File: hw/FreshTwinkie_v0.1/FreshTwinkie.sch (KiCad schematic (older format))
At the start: 54 parts, among them J1 USB_B_Micro, J2 USB_C_Receptacle, P1 USB_C_Plug, Q4 BSD840N, SW1 SW_Push, U1 INA260, U2 INA260, U5 STM32F072CBUx

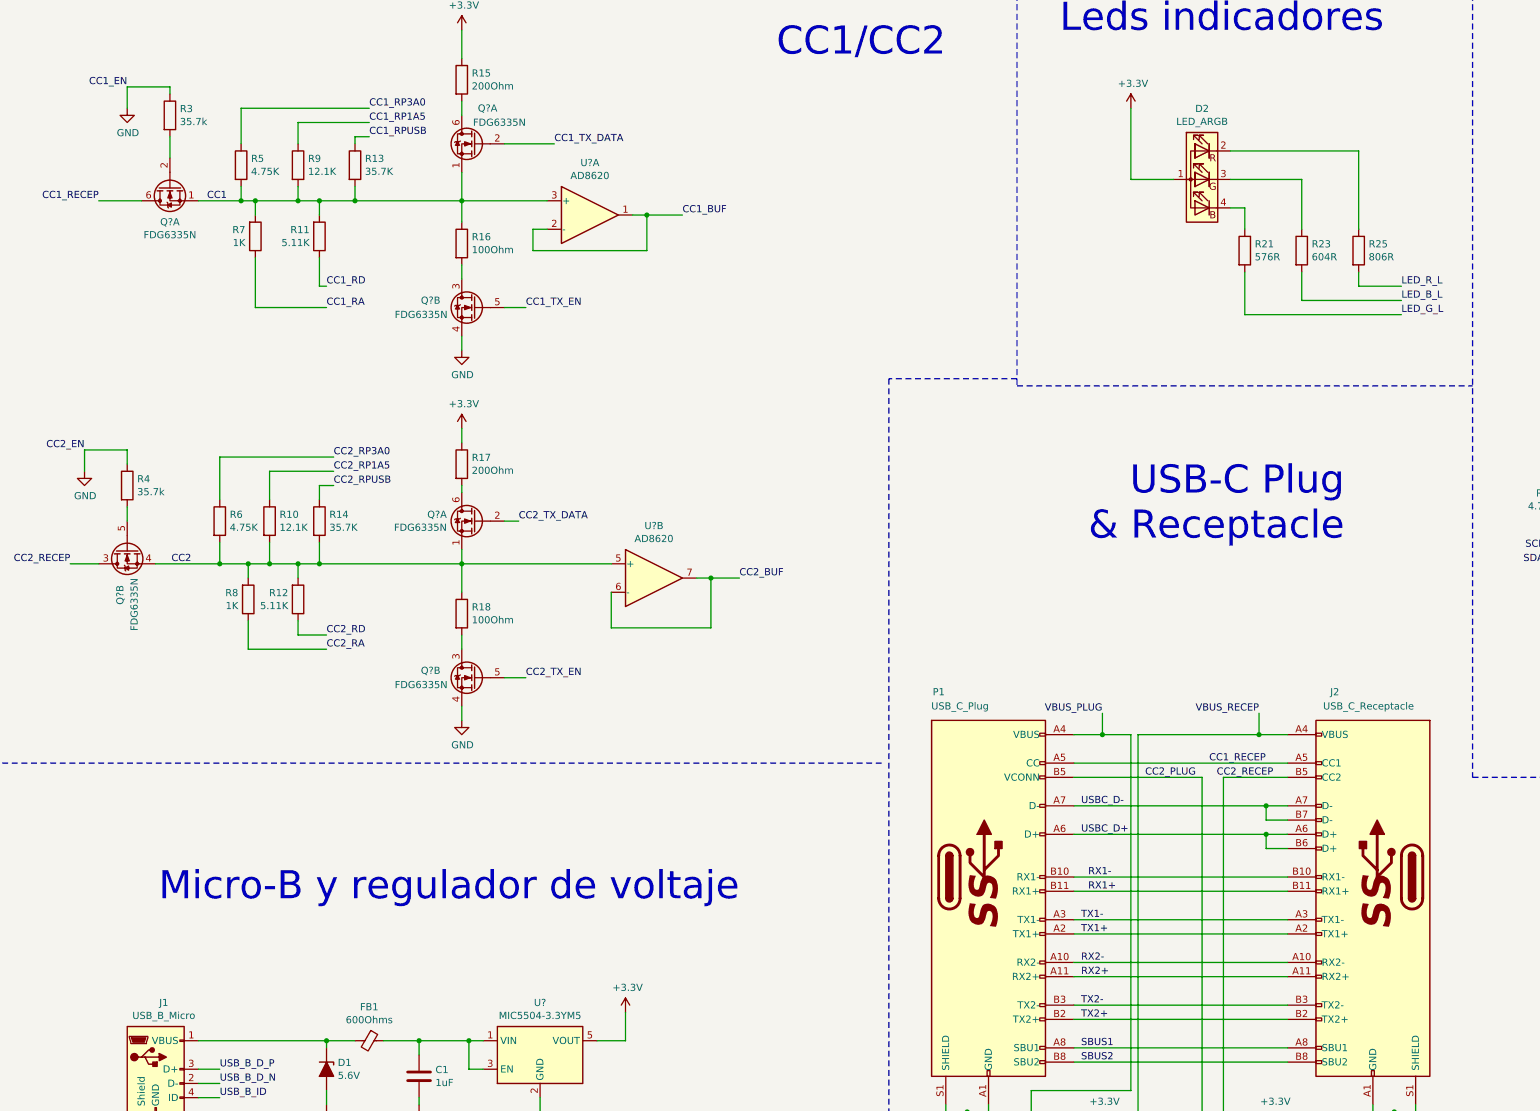
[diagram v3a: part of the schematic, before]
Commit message: changeLEDRvalor
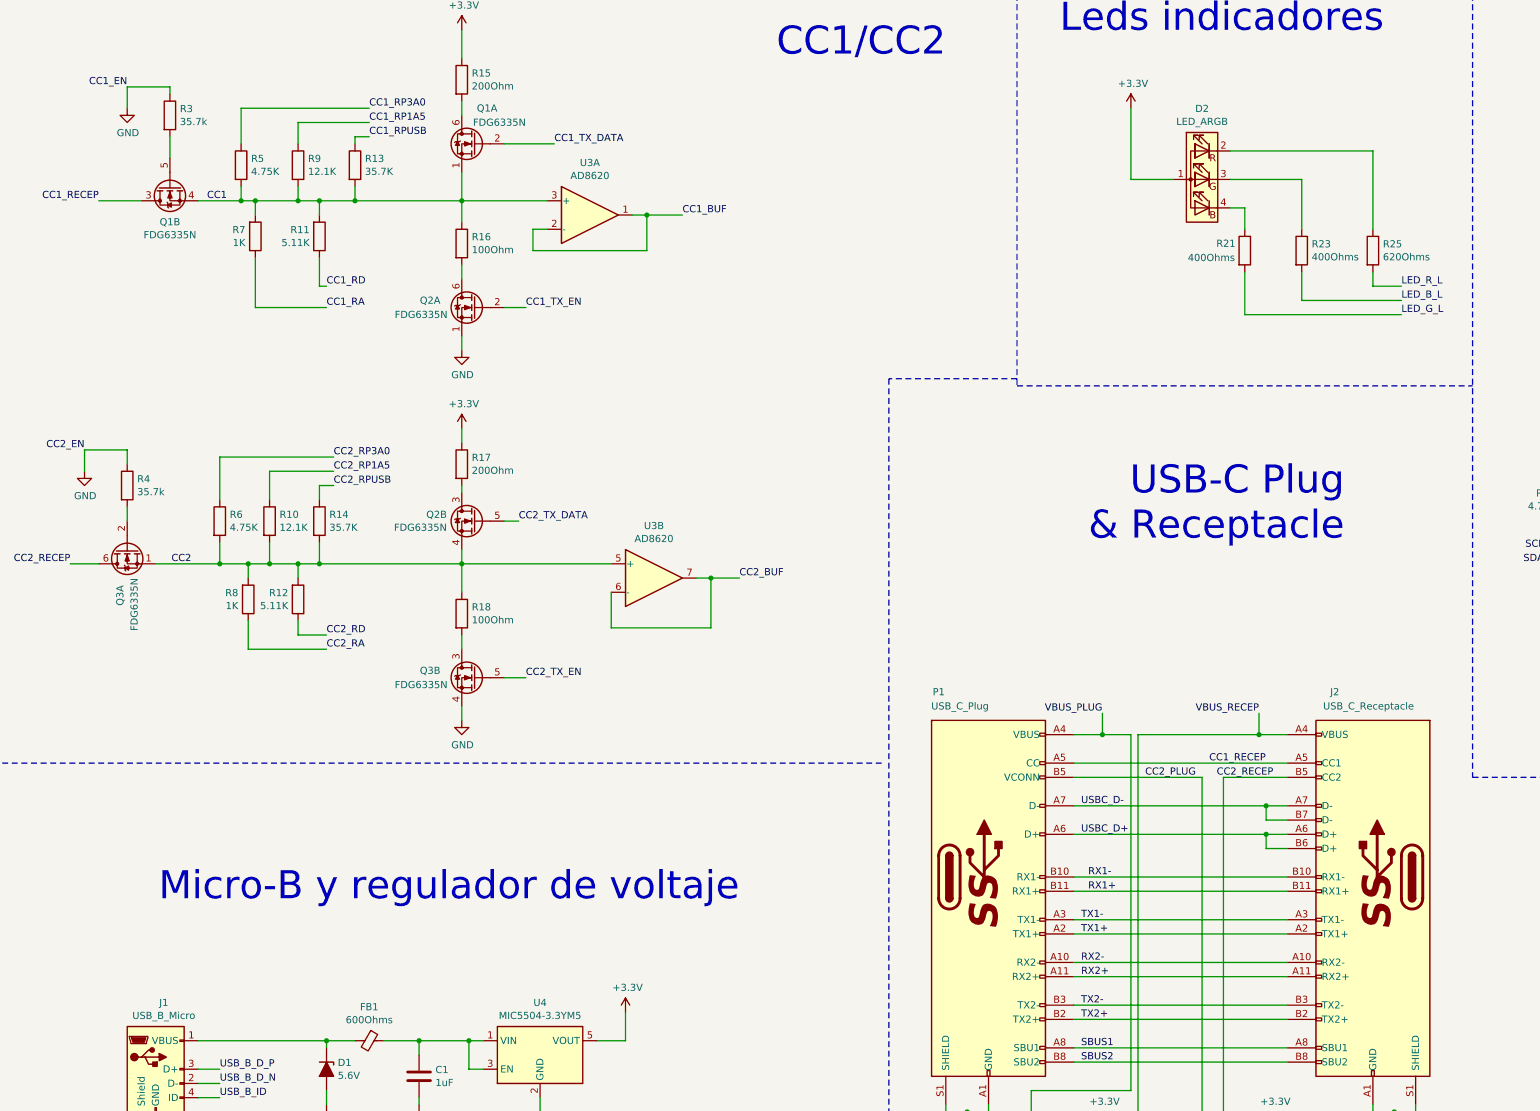
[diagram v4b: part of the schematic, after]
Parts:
- R21: value 576R -> 400Ohms
- R23: value 604R -> 400Ohms
- R25: value 806R -> 620Ohms
- gave numbers to parts that had none: 5
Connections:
- net CC1: now also Q1.4 (S); no longer Q1.1 (S)
- net CC1_RECEP: now also Q1.3 (D); no longer Q1.6 (D)
- net CC1_TX_EN: now also Q2.2 (G); no longer Q2.5 (G)
- net CC2: now also Q2.4 (S), Q3.1 (S); no longer Q2.1 (S), Q3.4 (S)
- net CC2_RECEP: now also Q3.6 (D); no longer Q3.3 (D)
- net CC2_TX_DATA: now also Q2.5 (G); no longer Q2.2 (G)
- net GND: now also Q2.1 (S); no longer Q2.4 (S)
- net at R3.2: now also Q1.5 (G); no longer Q1.2 (G)
- net at R16.2: now also Q2.6 (D); no longer Q2.3 (D)
- net at R4.2: now also Q3.2 (G); no longer Q3.5 (G)
- net at R17.2: now also Q2.3 (D); no longer Q2.6 (D)
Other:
- moved on the sheet: R25
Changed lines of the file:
@@
 U 1 1 5CA5AD96
 P 9600 2500
-F 0 "R21" H 9670 2546 50  0000 L CNN
-F 1 "576R" H 9670 2455 50  0000 L CNN
+F 0 "R21" H 9400 2550 50  0000 L CNN
+F 1 "400Ohms" H 9200 2450 50  0000 L CNN
 F 2 "gkl_dipol:R_0201" V 9530 2500 50  0001 C CNN
 F 3 "~" H 9600 2500 50  0001 C CNN
@@
 P 10000 2500
 F 0 "R23" H 10070 2546 50  0000 L CNN
-F 1 "604R" H 10070 2455 50  0000 L CNN
+F 1 "400Ohms" H 10070 2455 50  0000 L CNN
 F 2 "gkl_dipol:R_0201" V 9930 2500 50  0001 C CNN
 F 3 "~" H 10000 2500 50  0001 C CNN
@@
 L Device:R R25
 U 1 1 5CA5BD82
-P 10400 2500
-F 0 "R25" H 10470 2546 50  0000 L CNN
-F 1 "806R" H 10470 2455 50  0000 L CNN
-F 2 "gkl_dipol:R_0201" V 10330 2500 50  0001 C CNN
-F 3 "~" H 10400 2500 50  0001 C CNN
-F 4 "RC0201FR-07806RL" H 10400 2500 50  0001 C CNN "PN"
-F 5 "Yageo" H 10400 2500 50  0001 C CNN "Mfg"
-	1    10400 2500
+P 10500 2500
+F 0 "R25" H 10570 2546 50  0000 L CNN
+F 1 "620Ohms" H 10570 2455 50  0000 L CNN
+F 2 "gkl_dipol:R_0201" V 10430 2500 50  0001 C CNN
+F 3 "~" H 10500 2500 50  0001 C CNN
+F 4 "RC0201FR-07806RL" H 10500 2500 50  0001 C CNN "PN"
+F 5 "Yageo" H 10500 2500 50  0001 C CNN "Mfg"
+	1    10500 2500
 	1    0    0    -1
 $EndComp
@@
 	10000 2000 10000 2350
 Wire Wire Line
-	9500 1800 10400 1800
-Wire Wire Line
-	10400 1800 10400 2350
-Wire Wire Line
-	10400 2650 10400 2750
-Wire Wire Line
-	10400 2750 10700 2750
+	10500 2750 10700 2750
 Text Label 10700 2750 0    50   ~ 0
 LED_R_L
@@
 SBUS2
 $Comp
-L power:+3.3V #PWR?
+L power:+3.3V #PWR023
 U 1 1 60DEF09B
 P 9800 8650
-F 0 "#PWR?" H 9800 8500 50  0001 C CNN
+F 0 "#PWR023" H 9800 8500 50  0001 C CNN
 F 1 "+3.3V" H 9815 8823 50  0000 C CNN
 F 2 "" H 9800 8650 50  0001 C CNN
@@
 	9800 8650 9800 8700
 $Comp
-L power:GND #PWR?
+L power:GND #PWR027
 U 1 1 60E1F5E6
 P 9800 9550
-F 0 "#PWR?" H 9800 9300 50  0001 C CNN
+F 0 "#PWR027" H 9800 9300 50  0001 C CNN
 F 1 "GND" H 9805 9377 50  0000 C CNN
 F 2 "" H 9800 9550 50  0001 C CNN
@@
 	9800 9550 9800 9500
 $Comp
-L power:+3.3V #PWR?
+L power:+3.3V #PWR022
 U 1 1 60E77EB5
 P 8600 8650
-F 0 "#PWR?" H 8600 8500 50  0001 C CNN
+F 0 "#PWR022" H 8600 8500 50  0001 C CNN
 F 1 "+3.3V" H 8615 8823 50  0000 C CNN
 F 2 "" H 8600 8650 50  0001 C CNN
@@
 $EndComp
 $Comp
-L power:GND #PWR?
+L power:GND #PWR026
 U 1 1 60E78743
 P 8600 9550
-F 0 "#PWR?" H 8600 9300 50  0001 C CNN
+F 0 "#PWR026" H 8600 9300 50  0001 C CNN
 F 1 "GND" H 8605 9377 50  0000 C CNN
 F 2 "" H 8600 9550 50  0001 C CNN
@@
 	9300 9000 9400 9000
 $Comp
-L power:GND #PWR?
+L power:GND #PWR021
 U 1 1 60F8E5E0
 P 10650 8600
-F 0 "#PWR?" H 10650 8350 50  0001 C CNN
+F 0 "#PWR021" H 10650 8350 50  0001 C CNN
 F 1 "GND" H 10655 8427 50  0000 C CNN
 F 2 "" H 10650 8600 50  0001 C CNN
@@
 	10650 8550 10800 8550
 $Comp
-L power:GND #PWR?
+L power:GND #PWR020
 U 1 1 60FBB0CD
 P 7650 8600
-F 0 "#PWR?" H 7650 8350 50  0001 C CNN
+F 0 "#PWR020" H 7650 8350 50  0001 C CNN
 F 1 "GND" H 7655 8427 50  0000 C CNN
 F 2 "" H 7650 8600 50  0001 C CNN
@@
 	10450 9200 10200 9200
 $Comp
-L power:GND #PWR?
+L power:GND #PWR028
 U 1 1 61119AA6
 P 10600 9850
-F 0 "#PWR?" H 10600 9600 50  0001 C CNN
+F 0 "#PWR028" H 10600 9600 50  0001 C CNN
 F 1 "GND" H 10605 9677 50  0000 C CNN
 F 2 "" H 10600 9850 50  0001 C CNN
@@
 	10450 8850 10450 9200
 $Comp
-L power:+3.3V #PWR?
+L power:+3.3V #PWR025
 U 1 1 610FE570
 P 10450 8850
-F 0 "#PWR?" H 10450 8700 50  0001 C CNN
+F 0 "#PWR025" H 10450 8700 50  0001 C CNN
 F 1 "+3.3V" H 10465 9023 50  0000 C CNN
 F 2 "" H 10450 8850 50  0001 C CNN
@@
 	7100 11150 7150 11150
 $Comp
-L Transistor_FET:FDG6335N Q?
-U 1 1 61539F8C
+L Transistor_FET:FDG6335N Q1
+U 2 1 61539F8C
 P 2050 2050
-F 0 "Q?" V 2299 2050 50  0000 C CNN
+F 0 "Q1" V 2299 2050 50  0000 C CNN
 F 1 "FDG6335N" V 2390 2050 50  0000 C CNN
 F 2 "Package_TO_SOT_SMD:SOT-363_SC-70-6" H 2250 1975 50  0001 L CIN
 F 3 "http://www.gneic.com/product/datasheet/FDG6335N-1122853.pdf" H 2050 2050 50  0001 L CNN
-	1    2050 2050
+	2    2050 2050
 	0    -1   1    0
 $EndComp
@@
 	2050 1850 2050 1700
 $Comp
-L power:GND #PWR?
+L power:GND #PWR011
 U 1 1 615B931A
 P 1750 1500
-F 0 "#PWR?" H 1750 1250 50  0001 C CNN
+F 0 "#PWR011" H 1750 1250 50  0001 C CNN
 F 1 "GND" H 1755 1327 50  0000 C CNN
 F 2 "" H 1750 1500 50  0001 C CNN
@@
 	2650 2900 2650 2550
 $Comp
-L Amplifier_Operational:AD8620 U?
+L Amplifier_Operational:AD8620 U3
 U 1 1 6173663C
 P 5000 2250
-F 0 "U?" H 5000 2617 50  0000 C CNN
+F 0 "U3" H 5000 2617 50  0000 C CNN
 F 1 "AD8620" H 5000 2526 50  0000 C CNN
 F 2 "" H 5000 2250 50  0001 C CNN
@@
 	3100 2150 3350 2150
 $Comp
-L Transistor_FET:FDG6335N Q?
-U 2 1 6199D922
+L Transistor_FET:FDG6335N Q2
+U 1 1 6199D922
 P 4200 2900
-F 0 "Q?" H 4450 2950 50  0000 L CNN
+F 0 "Q2" H 4450 2950 50  0000 L CNN
 F 1 "FDG6335N" H 4400 2850 50  0000 L CNN
 F 2 "Package_TO_SOT_SMD:SOT-363_SC-70-6" H 4400 2825 50  0001 L CIN
 F 3 "http://www.gneic.com/product/datasheet/FDG6335N-1122853.pdf" H 4200 2900 50  0001 L CNN
-	2    4200 2900
+	1    4200 2900
 	-1   0    0    -1
 $EndComp
 $Comp
-L power:GND #PWR?
+L power:GND #PWR012
 U 1 1 61A5F316
 P 4100 3200
-F 0 "#PWR?" H 4100 2950 50  0001 C CNN
+F 0 "#PWR012" H 4100 2950 50  0001 C CNN
 F 1 "GND" H 4105 3027 50  0000 C CNN
 F 2 "" H 4100 3200 50  0001 C CNN
@@
 	4100 2150 4700 2150
 $Comp
-L Transistor_FET:FDG6335N Q?
+L Transistor_FET:FDG6335N Q1
 U 1 1 61C8DCCE
 P 4200 1750
-F 0 "Q?" H 4050 2000 50  0000 L CNN
+F 0 "Q1" H 4050 2000 50  0000 L CNN
 F 1 "FDG6335N" H 3850 1900 50  0000 L CNN
 F 2 "Package_TO_SOT_SMD:SOT-363_SC-70-6" H 4400 1675 50  0001 L CIN
@@
 	4100 1950 4100 2150
 $Comp
-L power:+3.3V #PWR?
+L power:+3.3V #PWR010
 U 1 1 61CB198B
 P 4100 950
-F 0 "#PWR?" H 4100 800 50  0001 C CNN
+F 0 "#PWR010" H 4100 800 50  0001 C CNN
 F 1 "+3.3V" H 4115 1123 50  0000 C CNN
 F 2 "" H 4100 950 50  0001 C CNN
@@
 CC1/CC2\n
 $Comp
-L Transistor_FET:FDG6335N Q?
-U 2 1 61ED81A1
+L Transistor_FET:FDG6335N Q3
+U 1 1 61ED81A1
 P 1750 4600
-F 0 "Q?" H 2000 4650 50  0000 L CNN
+F 0 "Q3" H 2000 4650 50  0000 L CNN
 F 1 "FDG6335N" H 1950 4550 50  0000 L CNN
 F 2 "Package_TO_SOT_SMD:SOT-363_SC-70-6" H 1950 4525 50  0001 L CIN
 F 3 "http://www.gneic.com/product/datasheet/FDG6335N-1122853.pdf" H 1750 4600 50  0001 L CNN
-	2    1750 4600
+	1    1750 4600
 	0    -1   1    0
 $EndComp
@@
 	1550 4700 1350 4700
 $Comp
-L power:GND #PWR?
+L power:GND #PWR014
 U 1 1 61F61D23
 P 1450 4050
-F 0 "#PWR?" H 1450 3800 50  0001 C CNN
+F 0 "#PWR014" H 1450 3800 50  0001 C CNN
 F 1 "GND" H 1455 3877 50  0000 C CNN
 F 2 "" H 1450 4050 50  0001 C CNN
@@
 	1450 3900 1450 4050
 $Comp
-L Amplifier_Operational:AD8620 U?
+L Amplifier_Operational:AD8620 U3
 U 2 1 61FCCB53
 P 5450 4800
-F 0 "U?" H 5450 5167 50  0000 C CNN
+F 0 "U3" H 5450 5167 50  0000 C CNN
 F 1 "AD8620" H 5450 5076 50  0000 C CNN
 F 2 "" H 5450 4800 50  0001 C CNN
@@
 	2950 5200 3150 5200
 $Comp
-L Transistor_FET:FDG6335N Q?
-U 1 1 62213D01
+L Transistor_FET:FDG6335N Q2
+U 2 1 62213D01
 P 4200 4400
-F 0 "Q?" H 4405 4446 50  0000 L CNN
+F 0 "Q2" H 4405 4446 50  0000 L CNN
 F 1 "FDG6335N" H 4405 4355 50  0000 L CNN
 F 2 "Package_TO_SOT_SMD:SOT-363_SC-70-6" H 4400 4325 50  0001 L CIN
 F 3 "http://www.gneic.com/product/datasheet/FDG6335N-1122853.pdf" H 4200 4400 50  0001 L CNN
-	1    4200 4400
+	2    4200 4400
 	-1   0    0    -1
 $EndComp
@@
 	4100 4700 3100 4700
 $Comp
-L power:+3.3V #PWR?
+L power:+3.3V #PWR013
 U 1 1 622E84EB
 P 4100 3750
-F 0 "#PWR?" H 4100 3600 50  0001 C CNN
+F 0 "#PWR013" H 4100 3600 50  0001 C CNN
 F 1 "+3.3V" H 4115 3923 50  0000 C CNN
 F 2 "" H 4100 3750 50  0001 C CNN
@@
 	4100 4900 4100 4700
 $Comp
-L Transistor_FET:FDG6335N Q?
+L Transistor_FET:FDG6335N Q3
 U 2 1 6233B865
 P 4200 5500
-F 0 "Q?" H 4450 5550 50  0000 L CNN
+F 0 "Q3" H 4450 5550 50  0000 L CNN
 F 1 "FDG6335N" H 4400 5450 50  0000 L CNN
 F 2 "Package_TO_SOT_SMD:SOT-363_SC-70-6" H 4400 5425 50  0001 L CIN
@@
 	4100 5300 4100 5200
 $Comp
-L power:GND #PWR?
+L power:GND #PWR015
 U 1 1 62365D65
 P 4100 5800
-F 0 "#PWR?" H 4100 5550 50  0001 C CNN
+F 0 "#PWR015" H 4100 5550 50  0001 C CNN
 F 1 "GND" H 4105 5627 50  0000 C CNN
 F 2 "" H 4100 5800 50  0001 C CNN
@@
 	7050 6100 500  6100
 $Comp
-L power:GND #PWR?
+L power:GND #PWR017
 U 1 1 62624492
 P 3150 8500
-F 0 "#PWR?" H 3150 8250 50  0001 C CNN
+F 0 "#PWR017" H 3150 8250 50  0001 C CNN
 F 1 "GND" H 3155 8327 50  0000 C CNN
 F 2 "" H 3150 8500 50  0001 C CNN
@@
 $EndComp
 $Comp
-L power:+3.3V #PWR?
+L power:+3.3V #PWR016
 U 1 1 6262473C
 P 5250 7850
-F 0 "#PWR?" H 5250 7700 50  0001 C CNN
+F 0 "#PWR016" H 5250 7700 50  0001 C CNN
 F 1 "+3.3V" H 5265 8023 50  0000 C CNN
 F 2 "" H 5250 7850 50  0001 C CNN
@@
 $EndComp
 $Comp
-L power:GND #PWR?
+L power:GND #PWR018
 U 1 1 6262503C
 P 3800 8500
-F 0 "#PWR?" H 3800 8250 50  0001 C CNN
+F 0 "#PWR018" H 3800 8250 50  0001 C CNN
 F 1 "GND" H 3805 8327 50  0000 C CNN
 F 2 "" H 3800 8500 50  0001 C CNN
@@
 $EndComp
 $Comp
-L power:GND #PWR?
+L power:GND #PWR024
 U 1 1 626252AD
 P 1850 8850
-F 0 "#PWR?" H 1850 8600 50  0001 C CNN
+F 0 "#PWR024" H 1850 8600 50  0001 C CNN
 F 1 "GND" H 1855 8677 50  0000 C CNN
 F 2 "" H 1850 8850 50  0001 C CNN
@@
 $EndComp
 $Comp
-L Regulator_Linear:MIC5504-3.3YM5 U?
+L Regulator_Linear:MIC5504-3.3YM5 U4
 U 1 1 626CB42B
 P 4650 8150
-F 0 "U?" H 4650 8517 50  0000 C CNN
+F 0 "U4" H 4650 8517 50  0000 C CNN
 F 1 "MIC5504-3.3YM5" H 4650 8426 50  0000 C CNN
 F 2 "Package_TO_SOT_SMD:SOT-23-5" H 4650 7750 50  0001 C CNN
@@
 	5250 8050 5250 7850
 $Comp
-L power:GND #PWR?
+L power:GND #PWR019
 U 1 1 627318D4
 P 4650 8550
-F 0 "#PWR?" H 4650 8300 50  0001 C CNN
+F 0 "#PWR019" H 4650 8300 50  0001 C CNN
 F 1 "GND" H 4655 8377 50  0000 C CNN
 F 2 "" H 4650 8550 50  0001 C CNN
@@
 Wire Wire Line
 	12850 3600 13000 3600
+Wire Wire Line
+	10500 2750 10500 2650
+Wire Wire Line
+	10500 2350 10500 1800
+Wire Wire Line
+	9500 1800 10500 1800
 $EndSCHEMATC

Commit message: generalchanges
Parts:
- removed Q4: BSD840N, gkl_housings_qfn:MOSFET_1.0x0.6mm, symbol Device:Q_NMOS_DGS
- added Q4: FDG6335N, Package_TO_SOT_SMD:SOT-363_SC-70-6, symbol Transistor_FET:FDG6335N
- renumbered C4 to C1, C5 to C4, C6 to C5, C7 to C6, C8 to C7, C1 to C8, D2 to D1, D1 to D2, FB2 to FB1, FB1 to FB2, J2 to J1, J1 to J2, R15 to R1, R23 to R10, R25 to R11, R17 to R12, R4 to R13, R22 to R14, R24 to R15, R6 to R16, R10 to R17, R14 to R18, R8 to R19, R3 to R2, R12 to R20, R18 to R21, R20 to R22, R19 to R23, R1 to R24, R5 to R3, R9 to R4, R13 to R5, R7 to R6, R11 to R7, R16 to R8, R21 to R9, U3 to U1, U5 to U2, U4 to U3, U1 to U4, U2 to U5
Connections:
- net BOOT: now also Q4.6 (D)
- net GND: now also Q4.1 (S)
- net USB_B_ID: now also Q4.2 (G)

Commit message: addPNdevicesPT1
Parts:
- C1, C6: footprint pkl_dipol:C_0402 -> (none); Mfg Samsung Electro-Mechanics -> (none); PN CL05A475MQ5NRNC -> (none)
- C2, C3, C7: footprint pkl_dipol:C_0201 -> (none); Mfg Samsung Electro-Mechanics -> (none); PN CL03A104KQ3NNNC -> (none)
- C4: footprint pkl_dipol:C_0201 -> (none); Mfg Samsung Electro-Mechanics -> (none); PN CL03B103KP3NNNC -> (none)
- C5, C8: footprint pkl_dipol:C_0402 -> (none); Mfg Samsung Electro-Mechanics -> (none); PN CL05A105MQ5NNNC -> (none)
- D1: footprint gkl_led:0404LED_RGB -> (none)
- D2: footprint Diode_SMD:D_0402_1005Metric -> (none)
- FB1, FB2: footprint pkl_dipol:L_0402 -> (none); Mfg Murata Electronics North America -> (none); PN BLM15AG601SN1D -> (none)
- J1: footprint Connector_USB:USB_C_Receptacle_Amphenol_12401610E4-2A -> (none); Mfg Amphenol ICC (Commercial Products) -> (none); PN 12401610E4#2A -> (none)
- J2: footprint Connector_USB:USB_Micro-B_GCT_USB3076-30-A -> (none); Mfg GCT -> (none); PN USB3076-30-A -> (none)
- P1: footprint Connector_USB:USB_C_Plug_Molex_105444 -> (none); Mfg Wurth Electronics Inc. -> (none); PN 632712000021 -> (none)
- Q1, Q2, Q3, Q4: value FDG6335N -> BSD840NH6327XTSA1; Mfg (none) -> Infineon; PN (none) -> C151516; Tienda (none) -> LCSC
- R1, R12: footprint gkl_dipol:R_0201 -> (none); Mfg Yageo -> (none); PN RC0201FR-07200RL -> (none)
- R10: footprint gkl_dipol:R_0201 -> (none); Mfg Yageo -> (none); PN RC0201FR-07604RL -> (none)
- R11: footprint gkl_dipol:R_0201 -> (none); Mfg Yageo -> (none); PN RC0201FR-07806RL -> (none)
- R13, R2: footprint gkl_dipol:R_0201 -> (none); Mfg Yageo -> (none); PN RC0201FR-07383KL -> (none)
- R14, R15: footprint gkl_dipol:R_0201 -> (none); Mfg Yageo -> (none); PN RC0201FR-072k1L -> (none)
- R16, R3: footprint gkl_dipol:R_0201 -> (none); Mfg Yageo -> (none); PN RC0201FR-074K75L -> (none)
- R17, R4: footprint gkl_dipol:R_0201 -> (none); Mfg Yageo -> (none); PN RC0201FR-0712K1L -> (none)
- R18, R5: footprint gkl_dipol:R_0201 -> (none); Mfg Yageo -> (none); PN RC0201FR-0735K7L -> (none)
- R19, R6: footprint gkl_dipol:R_0201 -> (none); Mfg Yageo -> (none); PN RC0201FR-071KL -> (none)
- R20, R7: footprint gkl_dipol:R_0201 -> (none); Mfg Yageo -> (none); PN RC0201FR-075K11L -> (none)
- R21, R8: footprint gkl_dipol:R_0201 -> (none); Mfg Yageo -> (none); PN RC0201FR-07100RL -> (none)
- R22, R23, R24: footprint gkl_dipol:R_0201 -> (none); Mfg Yageo -> (none); PN RC0201FR-0751k1L -> (none)
- R9: footprint gkl_dipol:R_0201 -> (none); Mfg Yageo -> (none); PN RC0201FR-07576RL -> (none)
- U1: value AD8620 -> AD8606ARMZ-REEL; Mfg (none) -> Analog Devices; PN (none) -> C459905; Tienda (none) -> LCSC
- U2: PN STM32F072CBU6 -> STM32F042C6T6TR; Tienda (none) -> Mouser
- U3: value MIC5504-3.3YM5 -> AP2112K; Mfg (none) -> Diodes Incorporated; PN (none) -> AP2112K-3.3TRG1; Tienda (none) -> Mouser
